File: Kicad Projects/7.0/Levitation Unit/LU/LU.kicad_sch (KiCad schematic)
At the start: 95 parts, among them IC1 1ED3322MC12NXUMA1, IC2 B0505S-2W, IC3 B0505S-2W, IC4 B0505S-2W, IC5 1ED3322MC12NXUMA1, J1 Conn_01x02_Male, J2 Conn_01x04_Pin, J3 Conn_01x02_Male, U1 LM7809_TO220, U10 6N137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

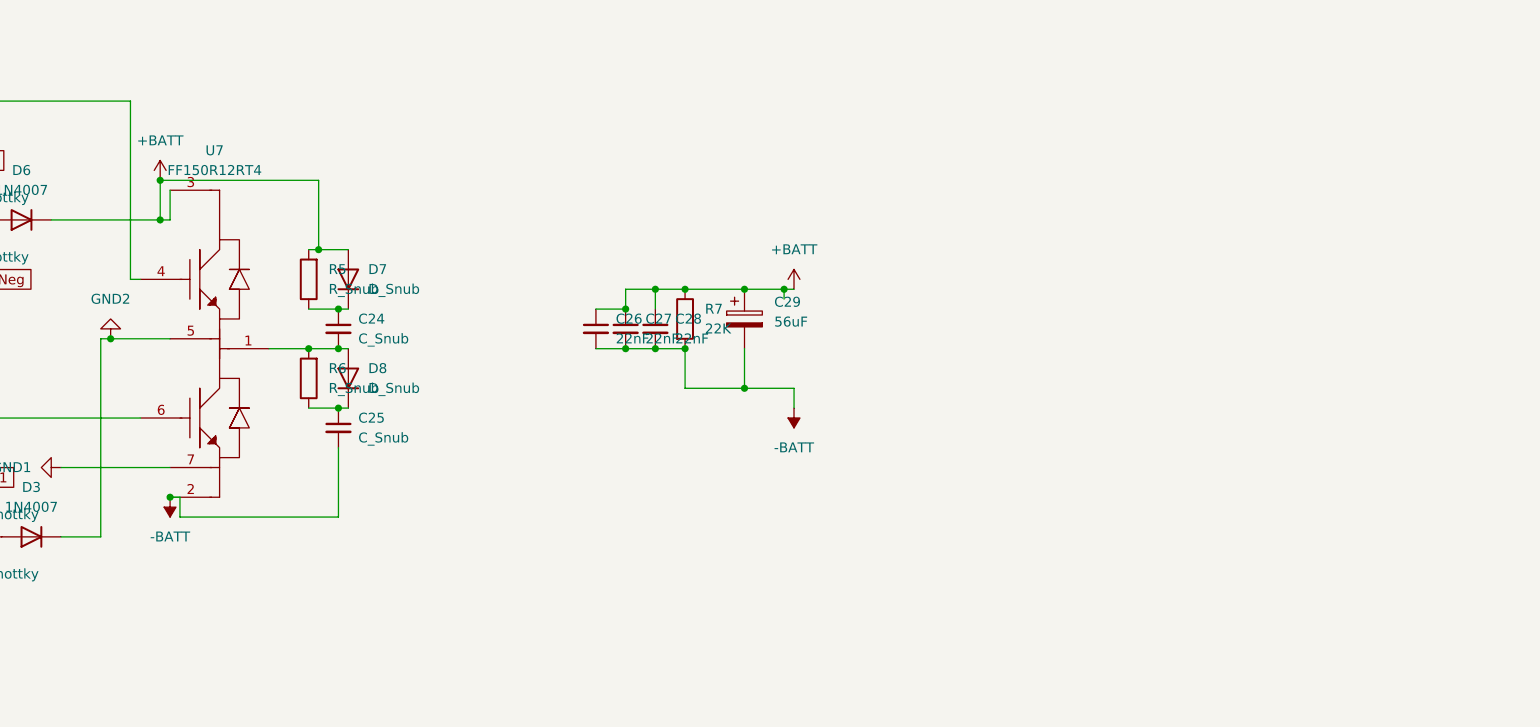
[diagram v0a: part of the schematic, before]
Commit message: Inverter 0 errors ready to export, LU fucked
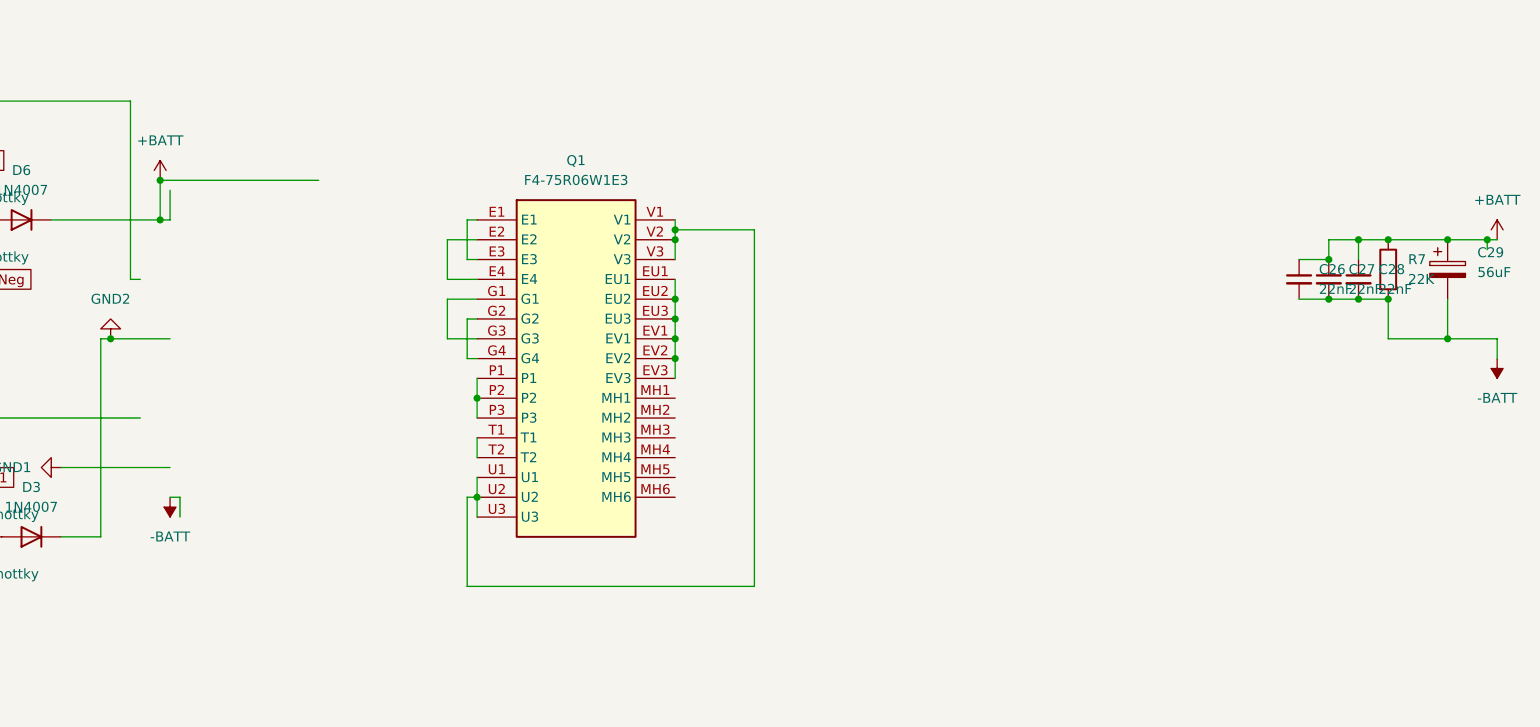
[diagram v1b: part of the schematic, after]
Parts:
- removed C24, C25: C_Snub, Capacitor_THT:C_Rect_L24.0mm_W8.3mm_P22.50mm_MKT, symbol Device:C_Small
- removed D7, D8: D_Snub, Diode_THT:D_DO-201AE_P15.24mm_Horizontal, symbol Device:D
- removed R5, R6: R_Snub, Resistor_THT:R_Box_L26.0mm_W5.0mm_P20.00mm, symbol Device:R
- removed U7: FF150R12RT4, FF300:FF300R12KS4, symbol FF300:FF300R12KS4
- added Q1: F4-75R06W1E3, IGBT:F475R06W1E3, symbol IGBT:F4-75R06W1E3
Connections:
- new net: Q1.E1, Q1.E3
- new net: Q1.E2, Q1.E4
- new net: Q1.EU1, Q1.EU2, Q1.EU3, Q1.EV1, Q1.EV2, Q1.EV3
- new net: Q1.G1, Q1.G3
- new net: Q1.G2, Q1.G4
- new net: Q1.P1, Q1.P2, Q1.P3
- new net: Q1.T1, Q1.T2
- new net: Q1.U1, Q1.U2, Q1.U3, Q1.V1, Q1.V2, Q1.V3
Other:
- moved on the sheet: C26, C27, C28, C29, R7
